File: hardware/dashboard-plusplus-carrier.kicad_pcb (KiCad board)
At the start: 4 copper layers, 95 x 55 mm, 56 parts, among them J1 XT30U-M, J10a ESP32-DEVKIT-A, J10b ESP32-DEVKIT-B, J13 DEBUG, J14 TRIP + EN, J15 SPARE, J16 SPARE N, J17 IGN + COOLANT, J18 SPARE S, J3 TFT-ILI9488, J6 LDR + FUEL, J8 GPS_PADS, J9 HALL, Q1 IRFR9540N, U4 DPP_DCDC_MODULE

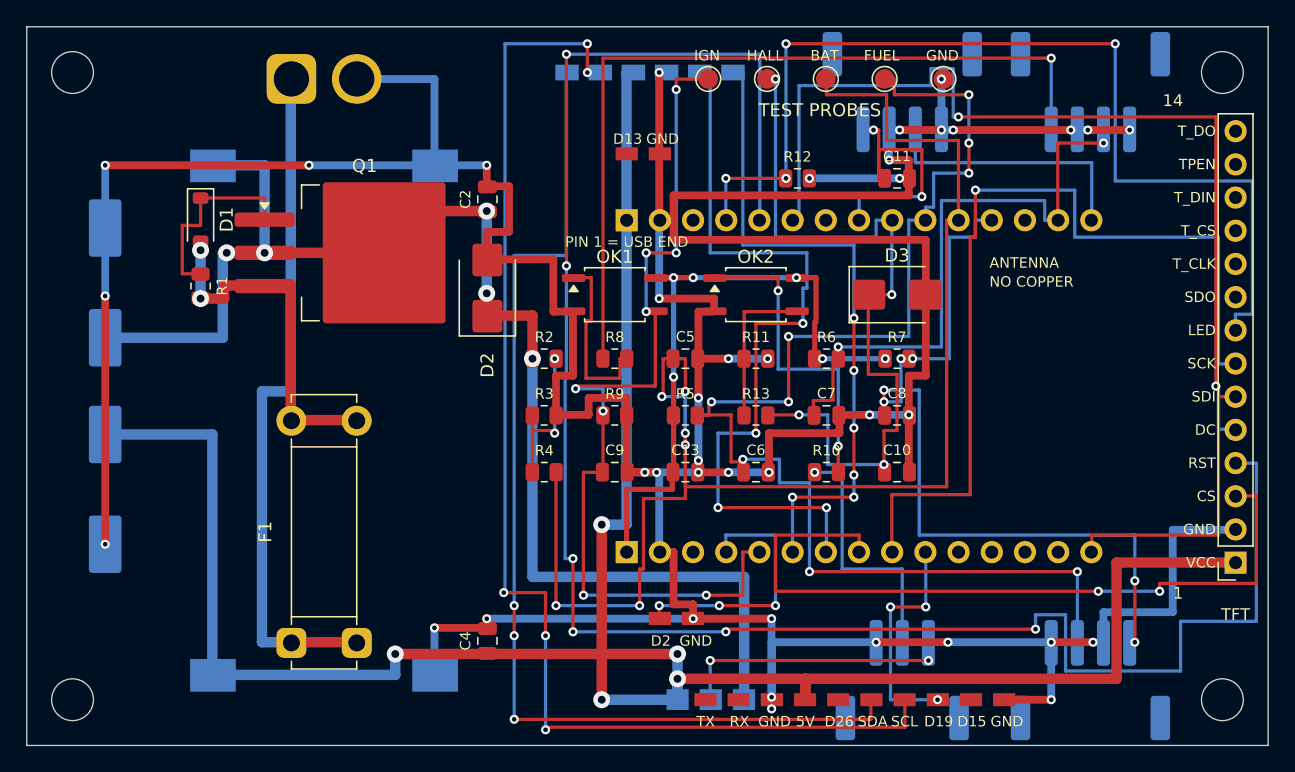
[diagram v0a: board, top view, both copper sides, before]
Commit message: Rip-up stranded nets by lifting foreign tracks, unrouted 7 -> 3
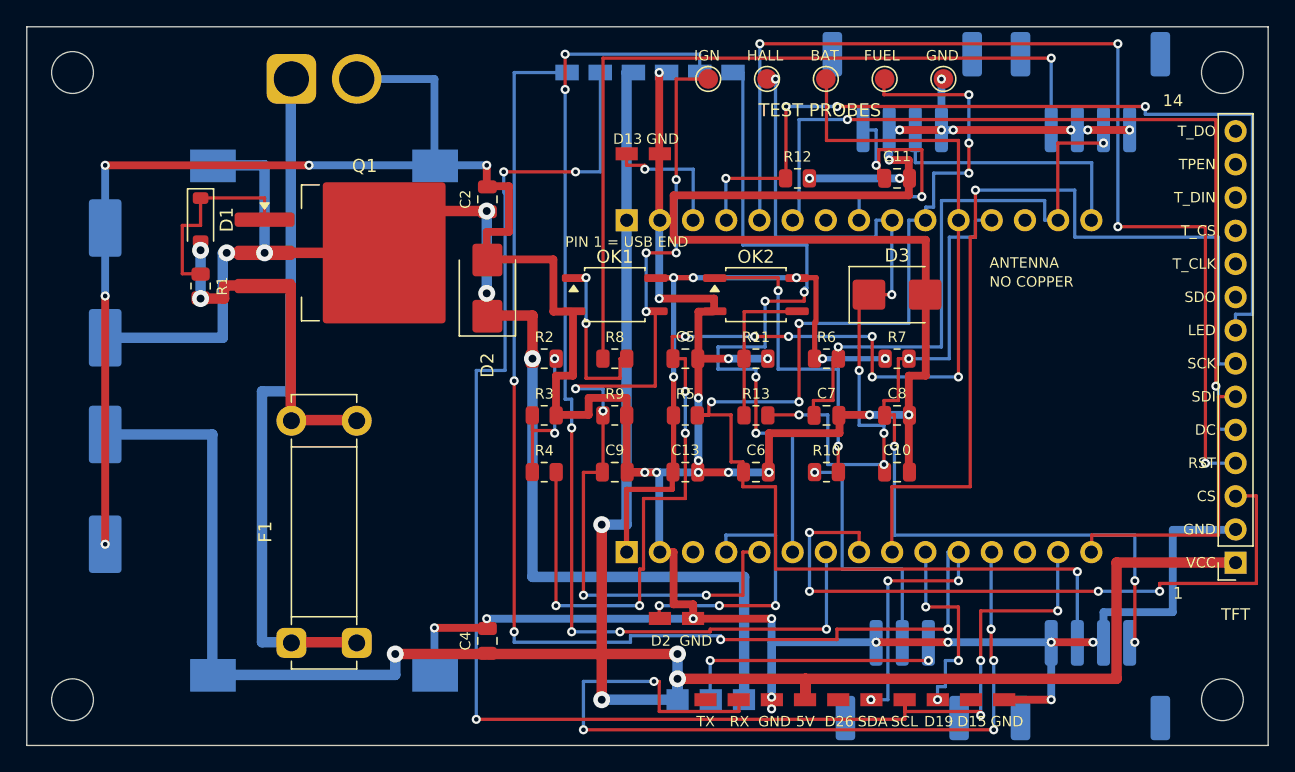
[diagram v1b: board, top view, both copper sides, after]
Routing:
- net TFT_RST: track 147.5 -> 81.8 mm, vias 6 -> 4
- net DBG_RX: track 0.00 -> 63.8 mm, vias 0 -> 5
- net SPARE_D21: track 82.1 -> 106.9 mm, vias 3 -> 7
- net SPARE_D22: track 94.9 -> 118.4 mm, vias 5 -> 6
- net GPS_TX: track 59.9 -> 81.8 mm, vias 4 -> 6
- net BAT_SNS: track 114.1 -> 99.1 mm, vias 6 -> 10
- net SPARE_D13: track 0.00 -> 10.0 mm, vias 0 -> 1
- net TFT_BL: track 76.8 -> 67.1 mm
- net TFT_DC: track 72.9 -> 65.1 mm
- net TFT_CS: track 57.5 -> 52.7 mm, vias 2 -> 4
- net GPS_RX: track 50.6 -> 54.8 mm, vias 6 -> 4
- net LDR_SNS: track 63.5 -> 59.7 mm, vias 6 -> 4
- net SPARE_D19: track 17.5 -> 15.3 mm
- net FUEL_SNS: track 100.8 -> 98.8 mm, vias 9 -> 7
- net IGN_LED: track 14.0 -> 13.2 mm, vias 0 -> 2
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
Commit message: Price wall cuts by leg length, pay debts depth-first: unrouted 3 -> 1
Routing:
- net V3V3: track 49.0 -> 100.5 mm, vias 6 -> 12
- net V5: track 178.7 -> 227.0 mm
- net DBG_TX: track 0.00 -> 39.0 mm, vias 0 -> 3
- net SPARE_D15: track 0.00 -> 33.9 mm, vias 0 -> 4
- net GND: track 382.7 -> 416.0 mm, vias 39 -> 40
- net DBG_RX: track 63.8 -> 37.0 mm, vias 5 -> 1
- net BAT_SNS: track 99.1 -> 87.7 mm, vias 10 -> 12
- net SPARE_D2: track 20.2 -> 10.0 mm, vias 3 -> 2
- net IGN_SENSE: track 70.7 -> 61.3 mm, vias 8 -> 6
- net FUEL_SNS: track 98.8 -> 104.0 mm
- net SPARE_D22: track 118.4 -> 120.5 mm
- net SPARE_D19: track 15.3 -> 17.3 mm, vias 3 -> 4
- net GPS_TX: track 81.8 -> 80.8 mm, vias 6 -> 8

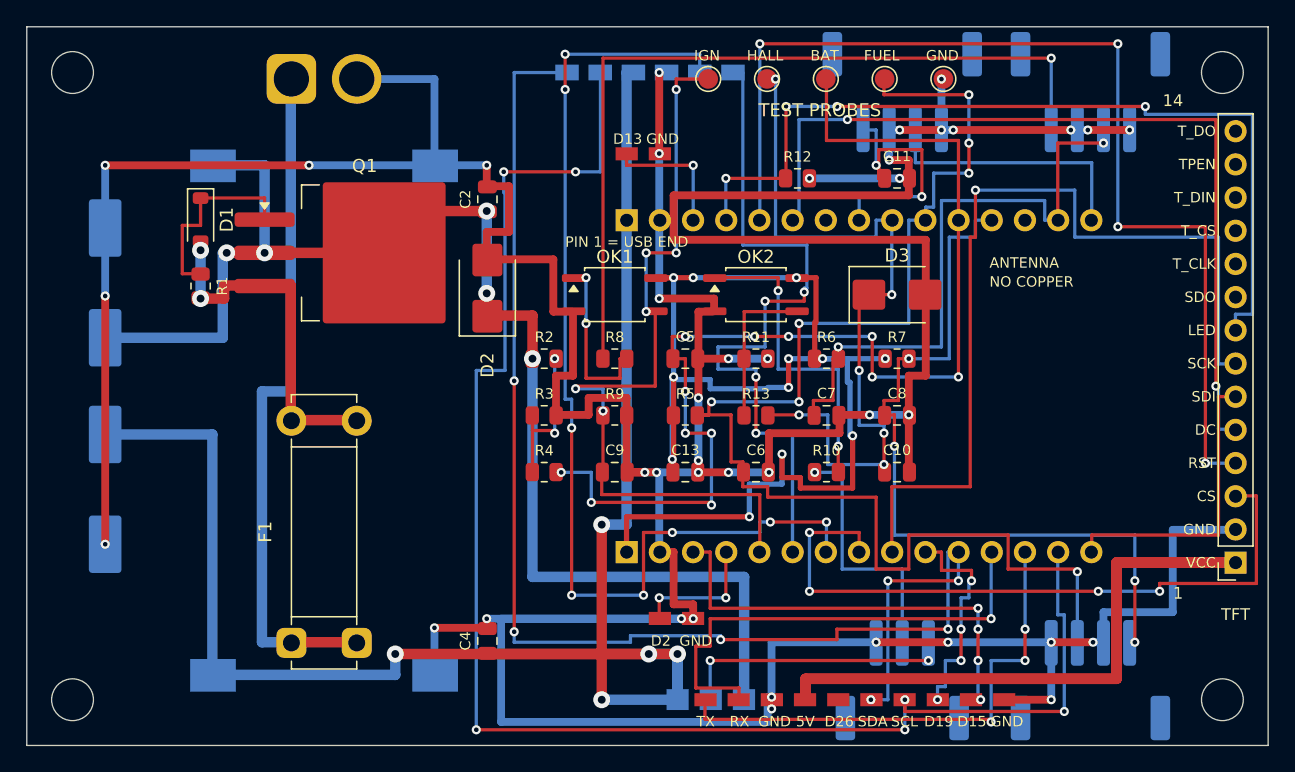
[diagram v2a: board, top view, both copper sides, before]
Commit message: Audit routing off the copper, not the books; weld cuts, no dup tracks
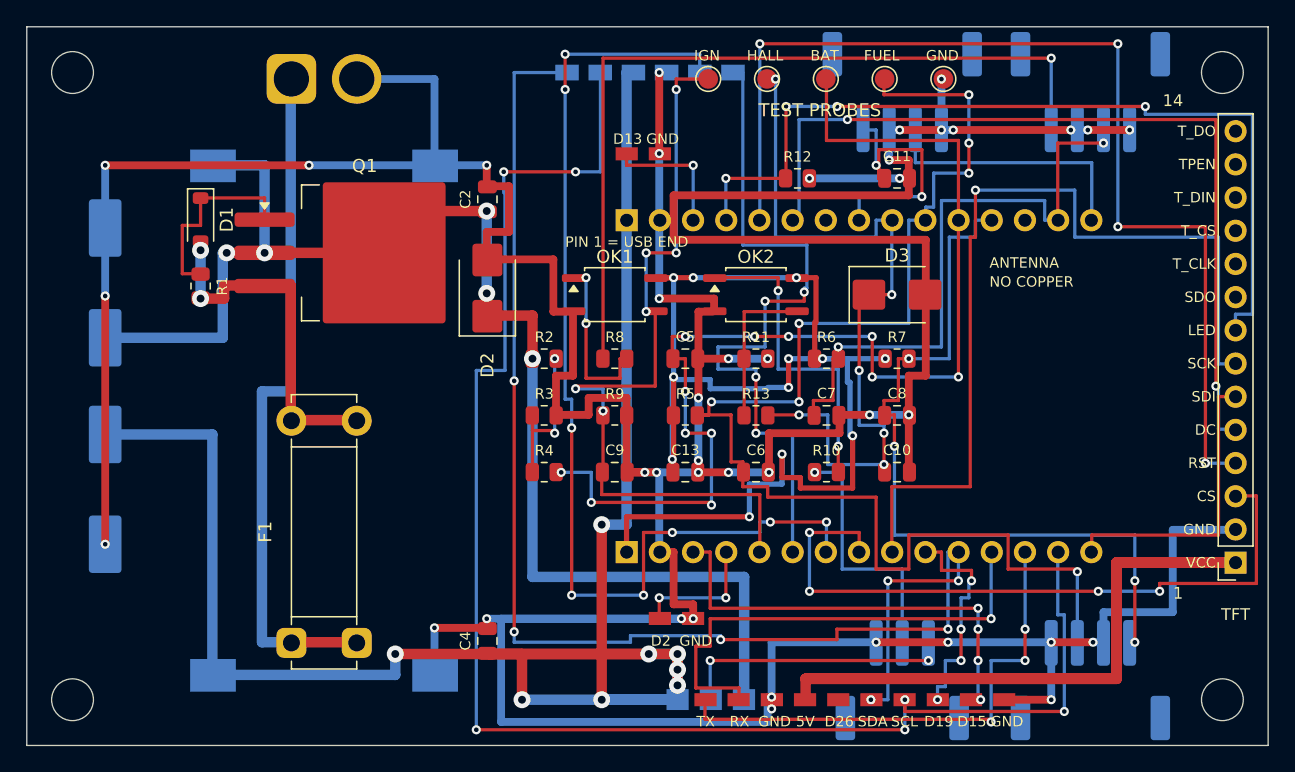
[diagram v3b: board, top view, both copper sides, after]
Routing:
- net V5: track 227.0 -> 312.2 mm, vias 5 -> 8

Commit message: Rip-up pays only copper that joins pads; unrouted nets 2 -> 1
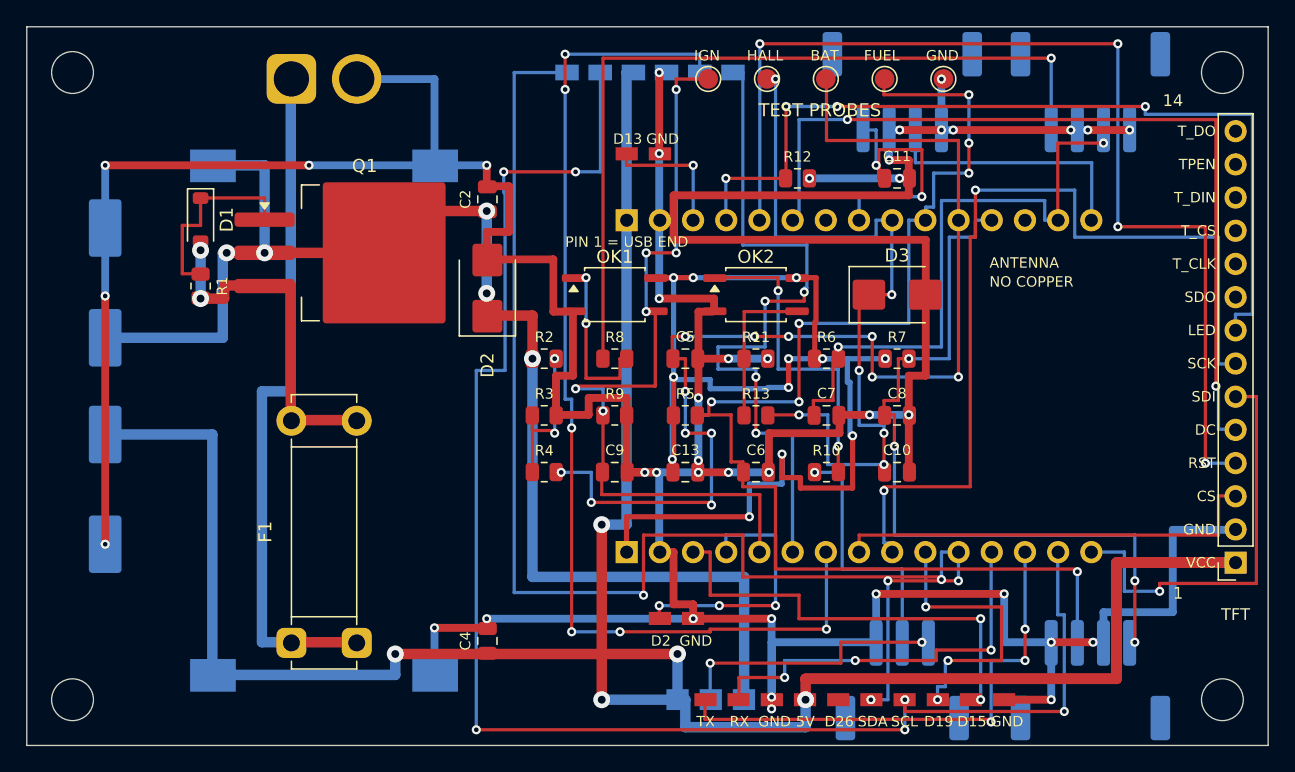
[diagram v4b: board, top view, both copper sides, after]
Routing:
- net V5: track 312.2 -> 221.5 mm, vias 8 -> 5
- net GND: track 416.0 -> 390.2 mm
- net TFT_CS: track 52.7 -> 32.9 mm, vias 4 -> 0
- net SPARE_D2: track 10.0 -> 20.2 mm, vias 2 -> 3
- net TFT_MOSI: track 22.7 -> 31.9 mm, vias 0 -> 1
- net DBG_RX: track 37.0 -> 30.4 mm, vias 1 -> 3
- net FUEL_SNS: track 104.0 -> 98.8 mm
- net SPARE_D19: track 17.3 -> 21.9 mm, vias 4 -> 3
- net TFT_SCK: track 67.1 -> 68.3 mm, vias 1 -> 2
- net SPARE_D21: track 106.9 -> 105.9 mm, vias 7 -> 5
- net GPS_TX: track 80.8 -> 81.8 mm, vias 8 -> 6
- net SPARE_D15: vias 4 -> 2

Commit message: Board routes clean: 0 violations, 0 unconnected; note it in PINOUT
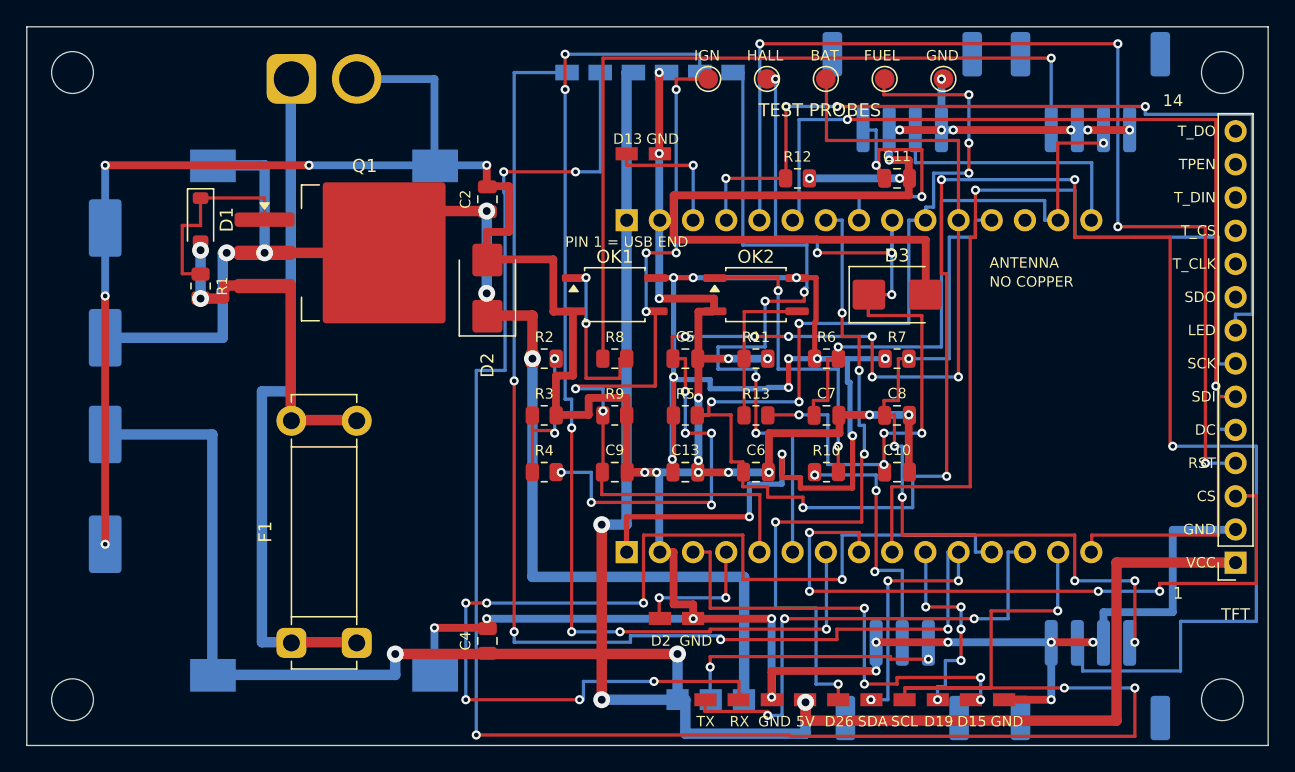
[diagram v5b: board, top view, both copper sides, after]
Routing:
- net FUEL_SNS: track 98.8 -> 181.5 mm, vias 7 -> 11
- net DBG_RX: track 30.4 -> 84.4 mm, vias 3 -> 7
- net SPARE_D26: track 0.00 -> 51.1 mm, vias 0 -> 5
- net V5: track 221.5 -> 183.8 mm
- net SPARE_D22: track 120.5 -> 154.7 mm
- net TFT_CS: track 32.9 -> 52.7 mm, vias 0 -> 4
- net GND: track 390.2 -> 371.1 mm
- net SPARE_D2: track 20.2 -> 10.0 mm, vias 3 -> 2
- net TFT_MOSI: track 31.9 -> 22.7 mm, vias 1 -> 0
- net HALL: track 59.4 -> 66.0 mm, vias 6 -> 8
- net SPARE_D19: track 21.9 -> 15.7 mm, vias 3 -> 5
- net TFT_SCK: track 68.3 -> 67.1 mm, vias 2 -> 1
- net SPARE_D21: track 105.9 -> 106.9 mm, vias 5 -> 7
- net SPARE_D15: track 33.9 -> 34.9 mm, vias 2 -> 4
- net DBG_TX: track 39.0 -> 38.0 mm
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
